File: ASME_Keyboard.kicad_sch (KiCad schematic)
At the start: 86 parts, among them SW1 SW_Push, SW10 SW_Push, SW11 SW_Push, SW12 SW_Push, SW13 SW_Push, SW14 SW_Push, SW15 SW_Push, SW16 SW_Push, SW17 SW_Push, SW18 SW_Push, SW19 SW_Push, SW2 SW_Push, SW20 SW_Push, SW21 SW_Push, SW22 SW_Push, SW23 SW_Push, SW24 SW_Push, SW25 SW_Push, SW26 SW_Push, SW27 SW_Push, SW28 SW_Push, SW29 SW_Push, SW3 SW_Push, SW30 SW_Push, SW31 SW_Push, SW32 SW_Push, SW33 SW_Push, SW34 SW_Push, SW35 SW_Push, SW36 SW_Push, SW37 SW_Push, SW38 SW_Push, SW39 SW_Push, SW4 SW_Push, SW40 SW_Push, SW41 SW_Push, SW42 SW_Push, SW5 SW_Push, SW6 SW_Push, SW7 SW_Push, SW8 SW_Push, SW9 SW_Push, U1 nice_nano, U2 nice_nano

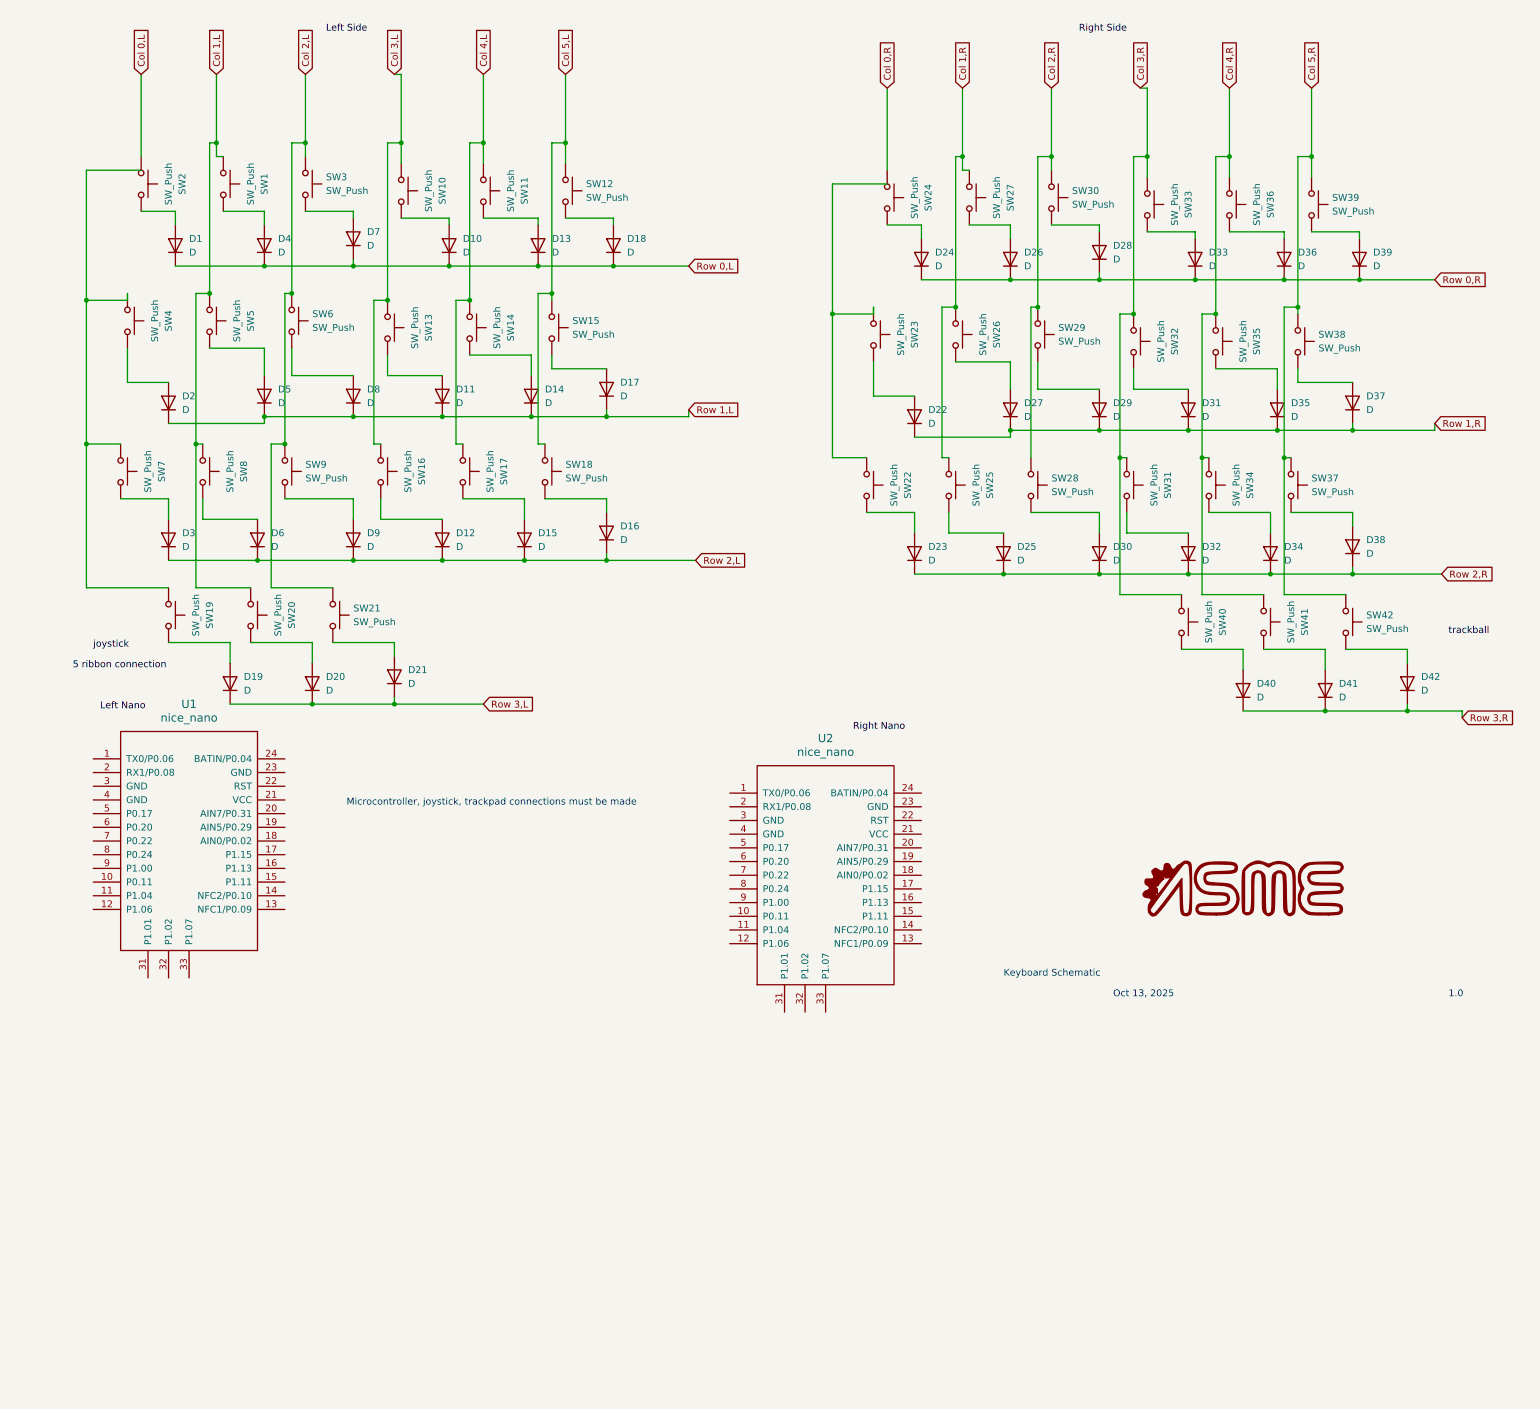
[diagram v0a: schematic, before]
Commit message: All PCB files
Need to change position file to not have negative numbers for rotations, match formatting to sent to manufacturing
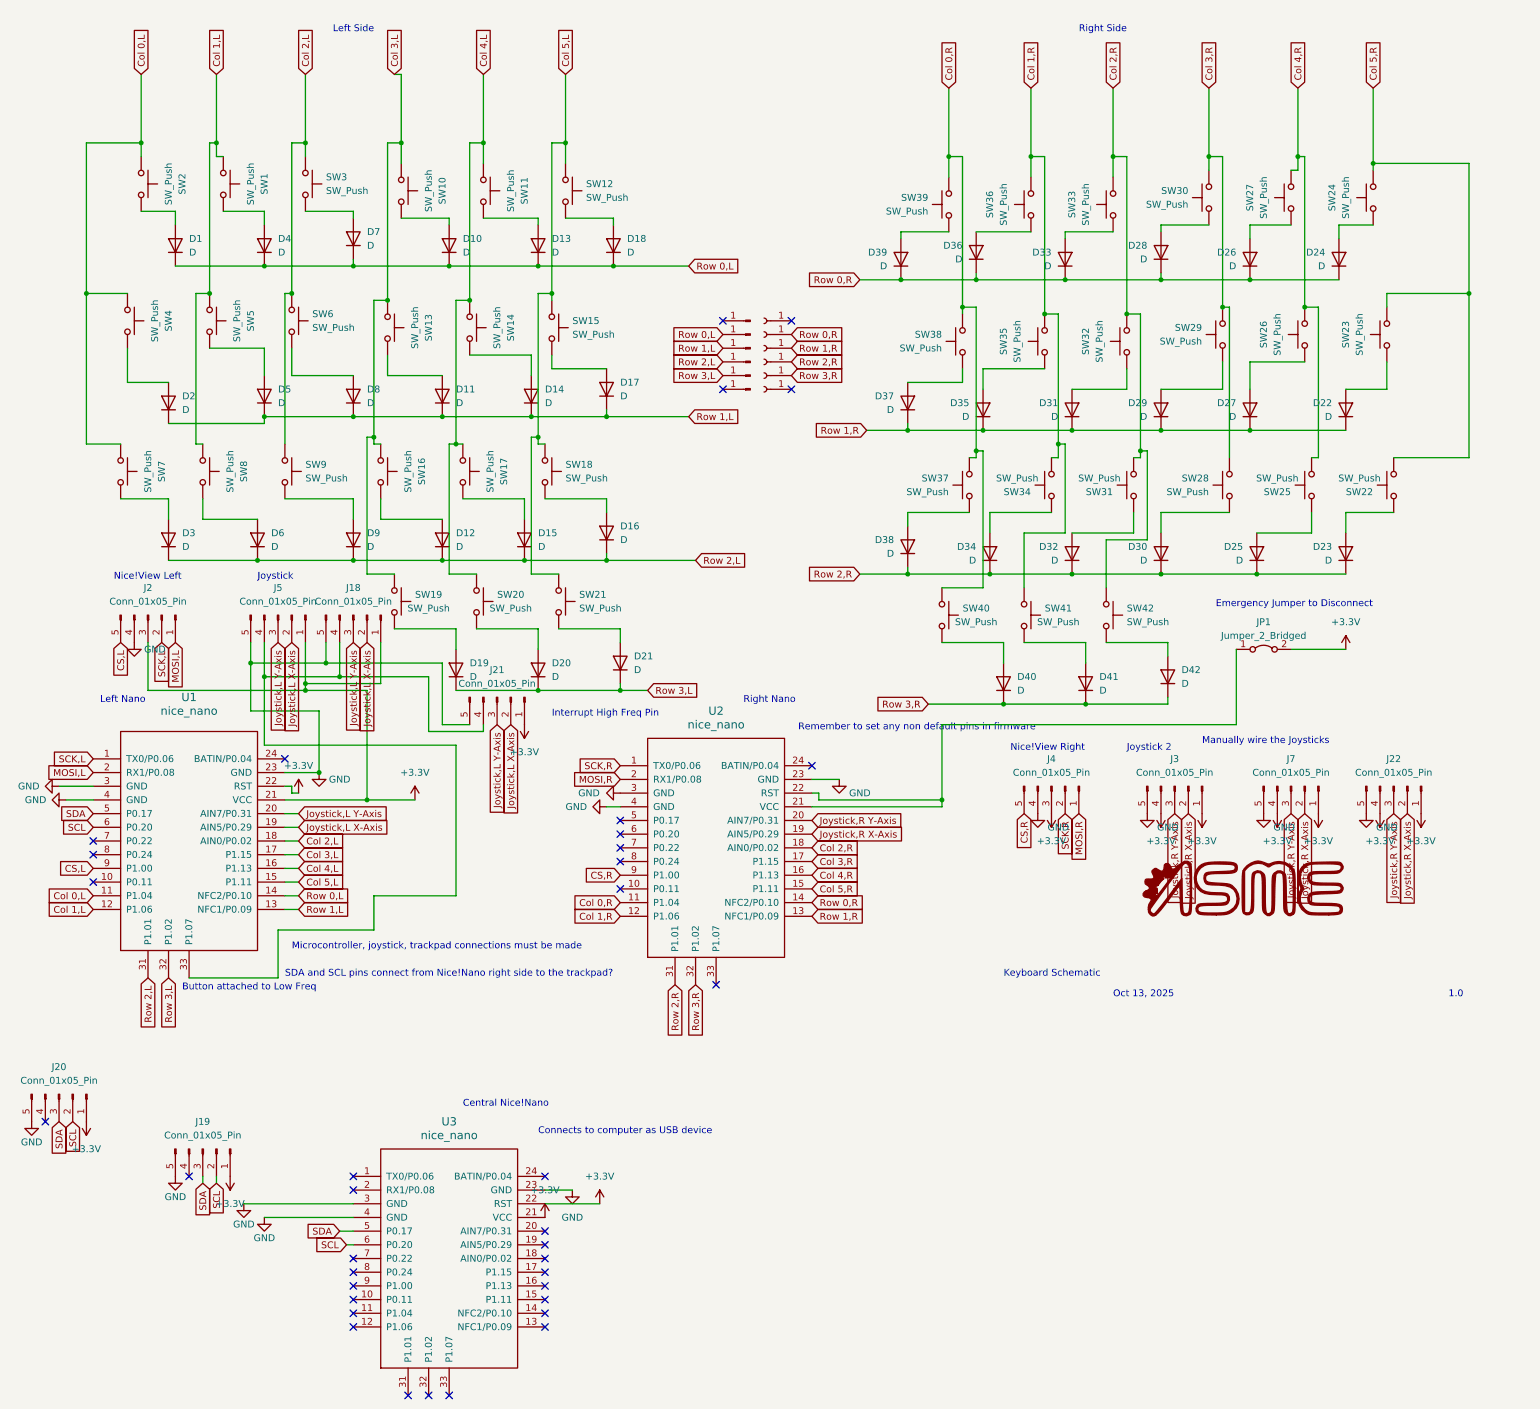
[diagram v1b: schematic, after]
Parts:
- added J1, J10, J11, J12, J8, J9: Conn_01x01_Pin, nice-nano-kicad-master:MF_Connectors-POGO_PIN_70-9150, symbol Connector:Conn_01x01_Pin
- added J13, J14, J15, J16, J17, J6: Conn_01x01_Socket, nice-nano-kicad-master:MF_Connectors-POGO_PIN_70-9150, symbol Connector:Conn_01x01_Socket
- added J18, J19, J20, J21, J22, J7: Conn_01x05_Pin, Connector_PinHeader_2.54mm:PinHeader_1x05_P2.54mm_Vertical, symbol Connector:Conn_01x05_Pin
- added J2, J4: Conn_01x05_Pin, nice_view:nice_view, symbol Connector:Conn_01x05_Pin
- added J3, J5: Conn_01x05_Pin, nice-nano-kicad-master:Joycon_edited_5pin, symbol Connector:Conn_01x05_Pin
- added JP1: Jumper_2_Bridged, Jumper:SolderJumper-2_P1.3mm_Open_Pad1.0x1.5mm, symbol Jumper:Jumper_2_Bridged
- added U3: nice_nano, nice-nano-kicad-master:nice_nano, symbol nice_nano:nice_nano
- D1, D10, D11, D12, D13, D14, D15, D16, D17, D18, D19, D2, D20, D21, D22, D23, D24, D25, D26, D27, D28, D29, D3, D30, D31, D32, D33, D34, D35, D36, D37, D38, D39, D4, D40, D41, D42, D5, D6, D7, D8, D9: footprint (none) -> Diode_SMD:D_1206_3216Metric
- SW1, SW10, SW11, SW12, SW13, SW14, SW15, SW16, SW17, SW18, SW19, SW2, SW20, SW21, SW22, SW23, SW24, SW25, SW26, SW27, SW28, SW29, SW3, SW30, SW31, SW32, SW33, SW34, SW35, SW36, SW37, SW38, SW39, SW4, SW40, SW41, SW42, SW5, SW6, SW7, SW8, SW9: footprint (none) -> keyswitches:Kailh_socket_MX
- U1, U2: footprint (none) -> nice-nano-kicad-master:nice_nano
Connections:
- net Col 0,L: now also SW4.1, SW7.1, U1.11 (P1.04)
- net Col 0,R: now also SW37.1, SW38.1, SW39.1, SW40.1, U2.11 (P1.04); no longer SW24.1
- net Col 1,L: now also U1.12 (P1.06); no longer SW20.1
- net Col 1,R: now also SW34.1, SW35.1, SW36.1, SW41.1, U2.12 (P1.06); no longer SW25.1, SW26.1, SW27.1
- net Col 2,L: now also U1.18 (AIN0/P0.02); no longer SW21.1
- net Col 2,R: now also SW31.1, SW32.1, SW33.1, SW42.1, U2.18 (AIN0/P0.02); no longer SW28.1, SW29.1, SW30.1
- net Col 3,L: now also SW19.1, U1.17 (P1.15)
- net Col 3,R: now also SW28.1, SW29.1, SW30.1, U2.17 (P1.15); no longer SW31.1, SW32.1, SW33.1, SW40.1
- net Col 4,L: now also SW20.1, U1.16 (P1.13)
- net Col 4,R: now also SW25.1, SW26.1, SW27.1, U2.16 (P1.13); no longer SW34.1, SW35.1, SW36.1, SW41.1
- net Col 5,L: now also SW21.1, U1.15 (P1.11)
- net Col 5,R: now also SW22.1, SW23.1, SW24.1, U2.15 (P1.11); no longer SW37.1, SW38.1, SW39.1, SW42.1
- net Row 0,L: now also U1.14 (NFC2/P0.10), J1.1 (Pin_1)
- net Row 0,R: now also U2.14 (NFC2/P0.10), J13.1 (Pin_1)
- net Row 1,L: now also U1.13 (NFC1/P0.09), J8.1 (Pin_1)
- net Row 1,R: now also U2.13 (NFC1/P0.09), J14.1 (Pin_1)
- net Row 2,L: now also U1.31 (P1.01), J9.1 (Pin_1)
- net Row 2,R: now also U2.31 (P1.01), J15.1 (Pin_1)
- net Row 3,L: now also U1.32 (P1.02), J10.1 (Pin_1)
- net Row 3,R: now also U2.32 (P1.02), J16.1 (Pin_1)
- net SCK,L: now reaches U1.1 (TX0/P0.06)
- net SCK,L: now also J2.2 (Pin_2)
- net Joystick,L X-Axis: now reaches U1.19 (AIN5/P0.29)
- net Joystick,L X-Axis: now also J18.2 (Pin_2), J21.2 (Pin_2), J5.2 (Pin_2)
- net MOSI,L: now reaches U1.2 (RX1/P0.08)
- net MOSI,L: now also J2.1 (Pin_1)
- net Joystick,L Y-Axis: now reaches U1.20 (AIN7/P0.31)
- net Joystick,L Y-Axis: now also J18.3 (Pin_3), J21.3 (Pin_3), J5.3 (Pin_3)
- net +3.3V: now reaches U1.21 (VCC)
- net +3.3V: now also U1.22 (RST), J18.1 (Pin_1), J19.1 (Pin_1), J2.3 (Pin_3), J20.1 (Pin_1), J21.1 (Pin_1), J22.1 (Pin_1), J22.4 (Pin_4), J3.1 (Pin_1), J3.4 (Pin_4), J4.3 (Pin_3), J5.1 (Pin_1), J7.1 (Pin_1), J7.4 (Pin_4), JP1.2 (B), U3.21 (VCC), U3.22 (RST)
- net GND: now reaches U1.23 (GND)
- net GND: now also U1.3 (GND), U1.4 (GND), U2.23 (GND), U2.3 (GND), U2.4 (GND), J18.5 (Pin_5), J19.5 (Pin_5), J2.4 (Pin_4), J20.5 (Pin_5), J21.5 (Pin_5), J22.5 (Pin_5), J3.5 (Pin_5), J4.4 (Pin_4), J5.5 (Pin_5), J7.5 (Pin_5), U3.23 (GND), U3.3 (GND), U3.4 (GND)
- net at U1.33 (P1.07): now also J18.4 (Pin_4), J21.4 (Pin_4), J5.4 (Pin_4)
- net SDA: now reaches U1.5 (P0.17)
- net SDA: now also J19.3 (Pin_3), J20.3 (Pin_3), U3.5 (P0.17)
- net SCL: now reaches U1.6 (P0.20)
- net SCL: now also J19.2 (Pin_2), J20.2 (Pin_2), U3.6 (P0.20)
- net CS,L: now reaches U1.9 (P1.00)
- net CS,L: now also J2.5 (Pin_5)
- net SCK,R: now reaches U2.1 (TX0/P0.06)
- net SCK,R: now also J4.2 (Pin_2)
- net Joystick,R X-Axis: now reaches U2.19 (AIN5/P0.29)
- net Joystick,R X-Axis: now also J22.2 (Pin_2), J3.2 (Pin_2), J7.2 (Pin_2)
- net MOSI,R: now reaches U2.2 (RX1/P0.08)
- net MOSI,R: now also J4.1 (Pin_1)
- net Joystick,R Y-Axis: now reaches U2.20 (AIN7/P0.31)
- net Joystick,R Y-Axis: now also J22.3 (Pin_3), J3.3 (Pin_3), J7.3 (Pin_3)
- net at U2.21 (VCC): now also U2.22 (RST), JP1.1 (A)
- net CS,R: now reaches U2.9 (P1.00)
- net CS,R: now also J4.5 (Pin_5)
- no-connect marks 0 -> 37
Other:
- note added: "Button attached to Low Freq"
- note added: "Central Nice!Nano"
- note added: "Connects to computer as USB device"
- note added: "Emergency Jumper to Disconnect"
- note added: "Interrupt High Freq Pin"
- note added: "Joystick"
- note added: "Joystick 2"
- note added: "Left Nano"
- note added: "Left Side"
- note added: "Manually wire the Joysticks"
- note added: "Nice!View Left"
- note added: "Nice!View Right"
- note added: "Remember to set any non default pins in firmware"
- note added: "Right Nano"
- note added: "Right Side"
- note added: "SDA and SCL pins connect from Nice!Nano right side to the trackpad?"
- moved on the sheet: D19, D20, D21, D22, D23, D24, D25, D26, D27, D28, D29, D30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
